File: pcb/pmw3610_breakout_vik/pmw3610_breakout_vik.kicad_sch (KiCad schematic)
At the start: 13 parts, among them J1 Conn_01x08, U1 MCP1700T-1802E/TT, U2 PMW3610

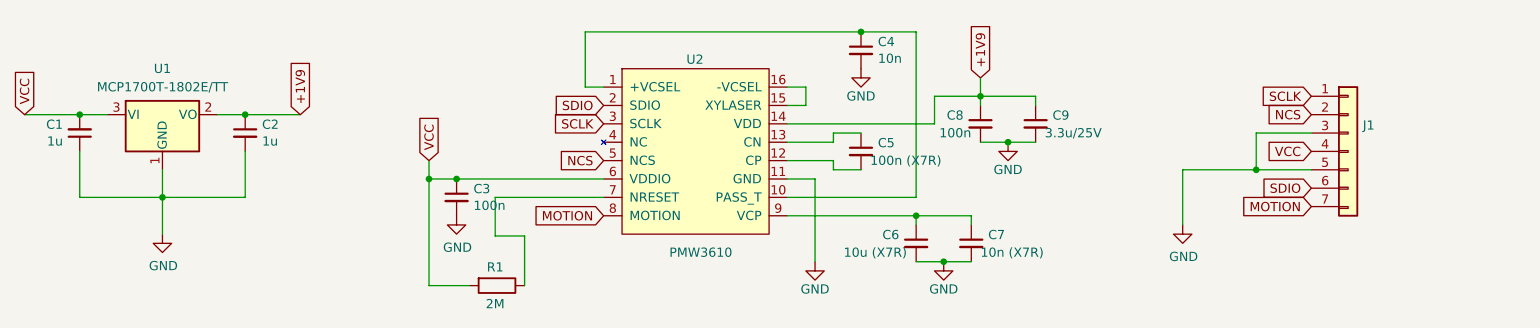
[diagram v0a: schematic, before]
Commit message: Update PMW3610 breakout
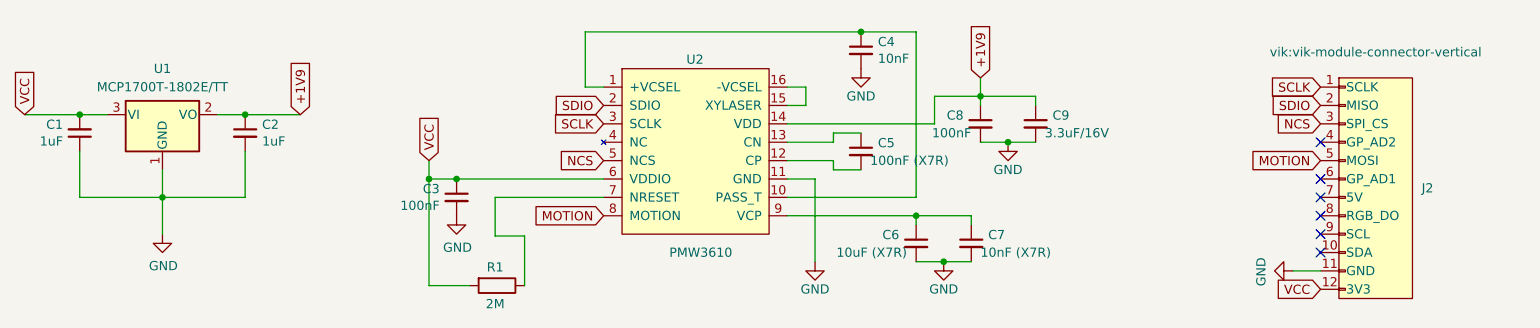
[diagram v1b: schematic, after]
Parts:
- removed J1: Conn_01x08, roBa:pmw3610_connector_b, symbol Connector_Generic:Conn_01x06
- added J2: vik-module-connector, vik:vik-module-connector-vertical, symbol vik:vik-module-connector
- C1: value 1u -> 1uF; LCSC C14663 -> (none)
- C2: value 1u -> 1uF; LCSC C15849 -> (none)
- C3, C8: value 100n -> 100nF; LCSC C19666 -> (none)
- C4: value 10n -> 10nF; LCSC C19666 -> (none)
- C5: value 100n (X7R) -> 100nF (X7R); LCSC C19666 -> (none)
- C6: value 10u (X7R) -> 10uF (X7R); LCSC C19666 -> (none)
- C7: value 10n (X7R) -> 10nF (X7R); LCSC C19666 -> (none)
- C9: value 3.3u/25V -> 3.3uF/16V; LCSC C19666 -> (none)
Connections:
- net GND: now also J2.11 (GND)
- net MOTION: now also J2.5 (MOSI)
- net NCS: now also J2.3 (SPI_CS)
- net SCLK: now also J2.1 (SCLK)
- net SDIO: now also J2.2 (MISO)
- net VCC: now also J2.12 (3V3)
- no-connect marks 0 -> 6
